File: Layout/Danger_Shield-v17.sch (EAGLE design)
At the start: 35 parts, among them U1 ARDUINO_SHIELD, U2 74LS595N, U4 TMP36

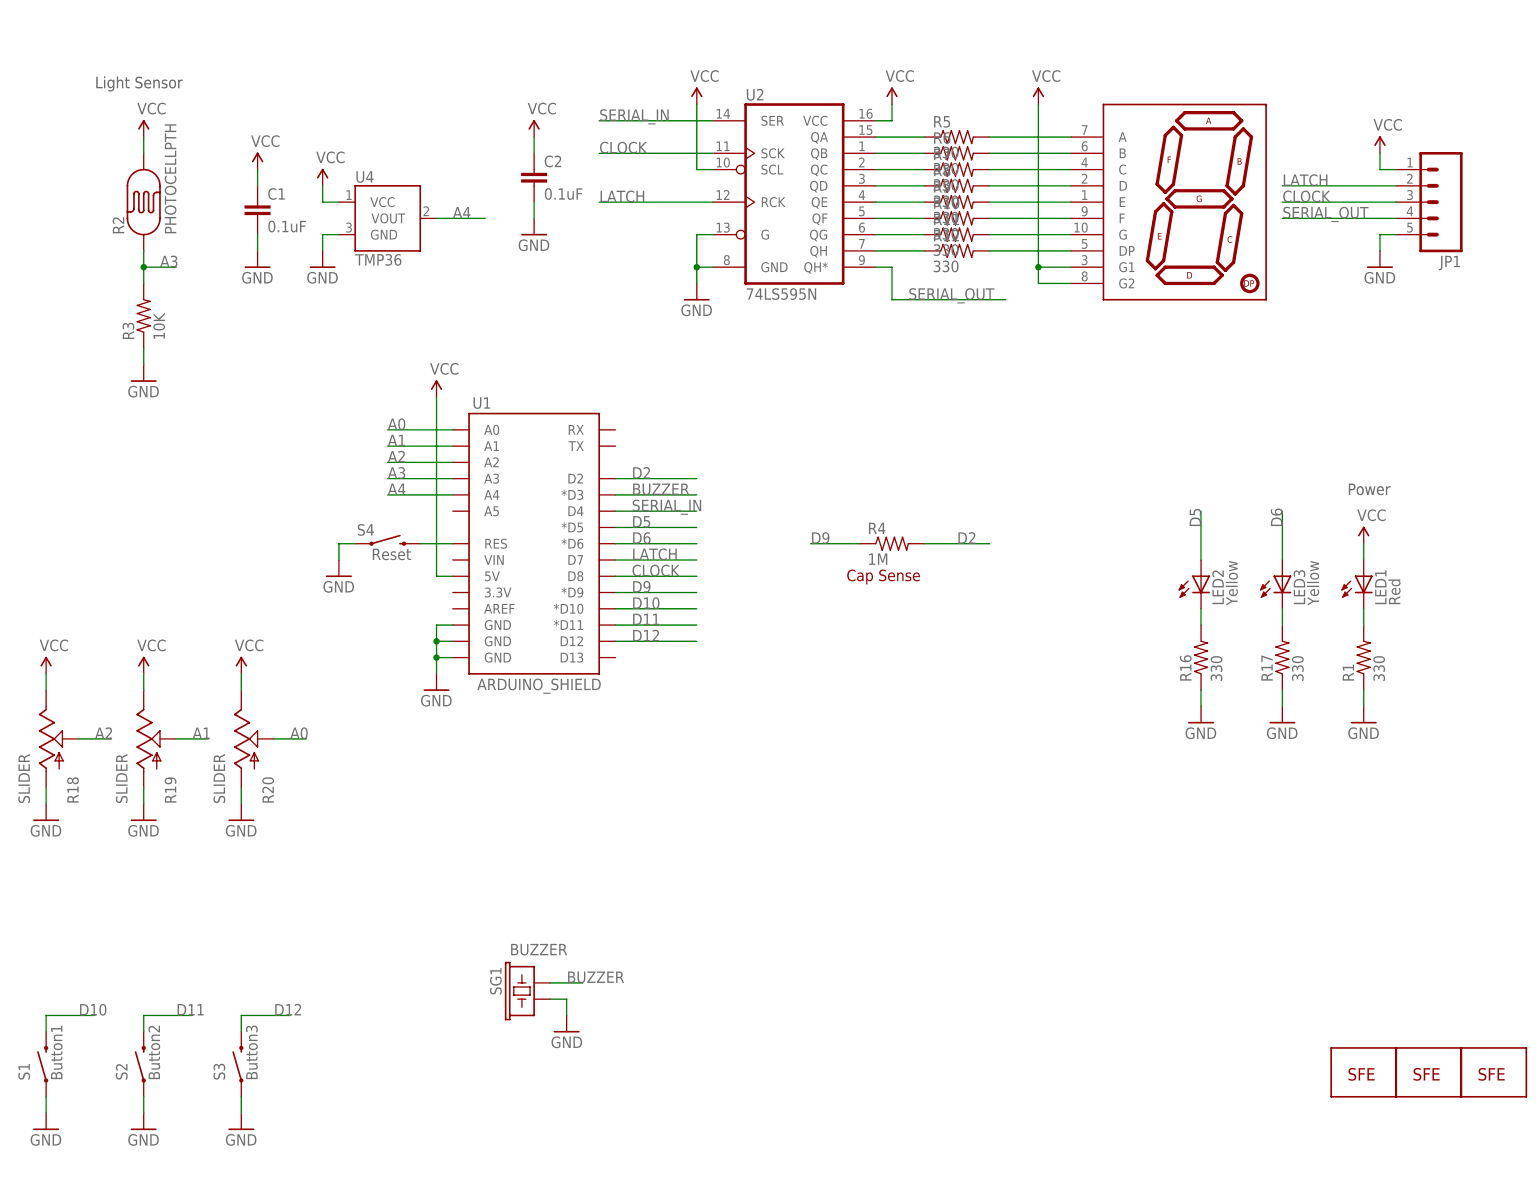
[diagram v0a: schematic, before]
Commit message: Added CC license to schematic and PCB.
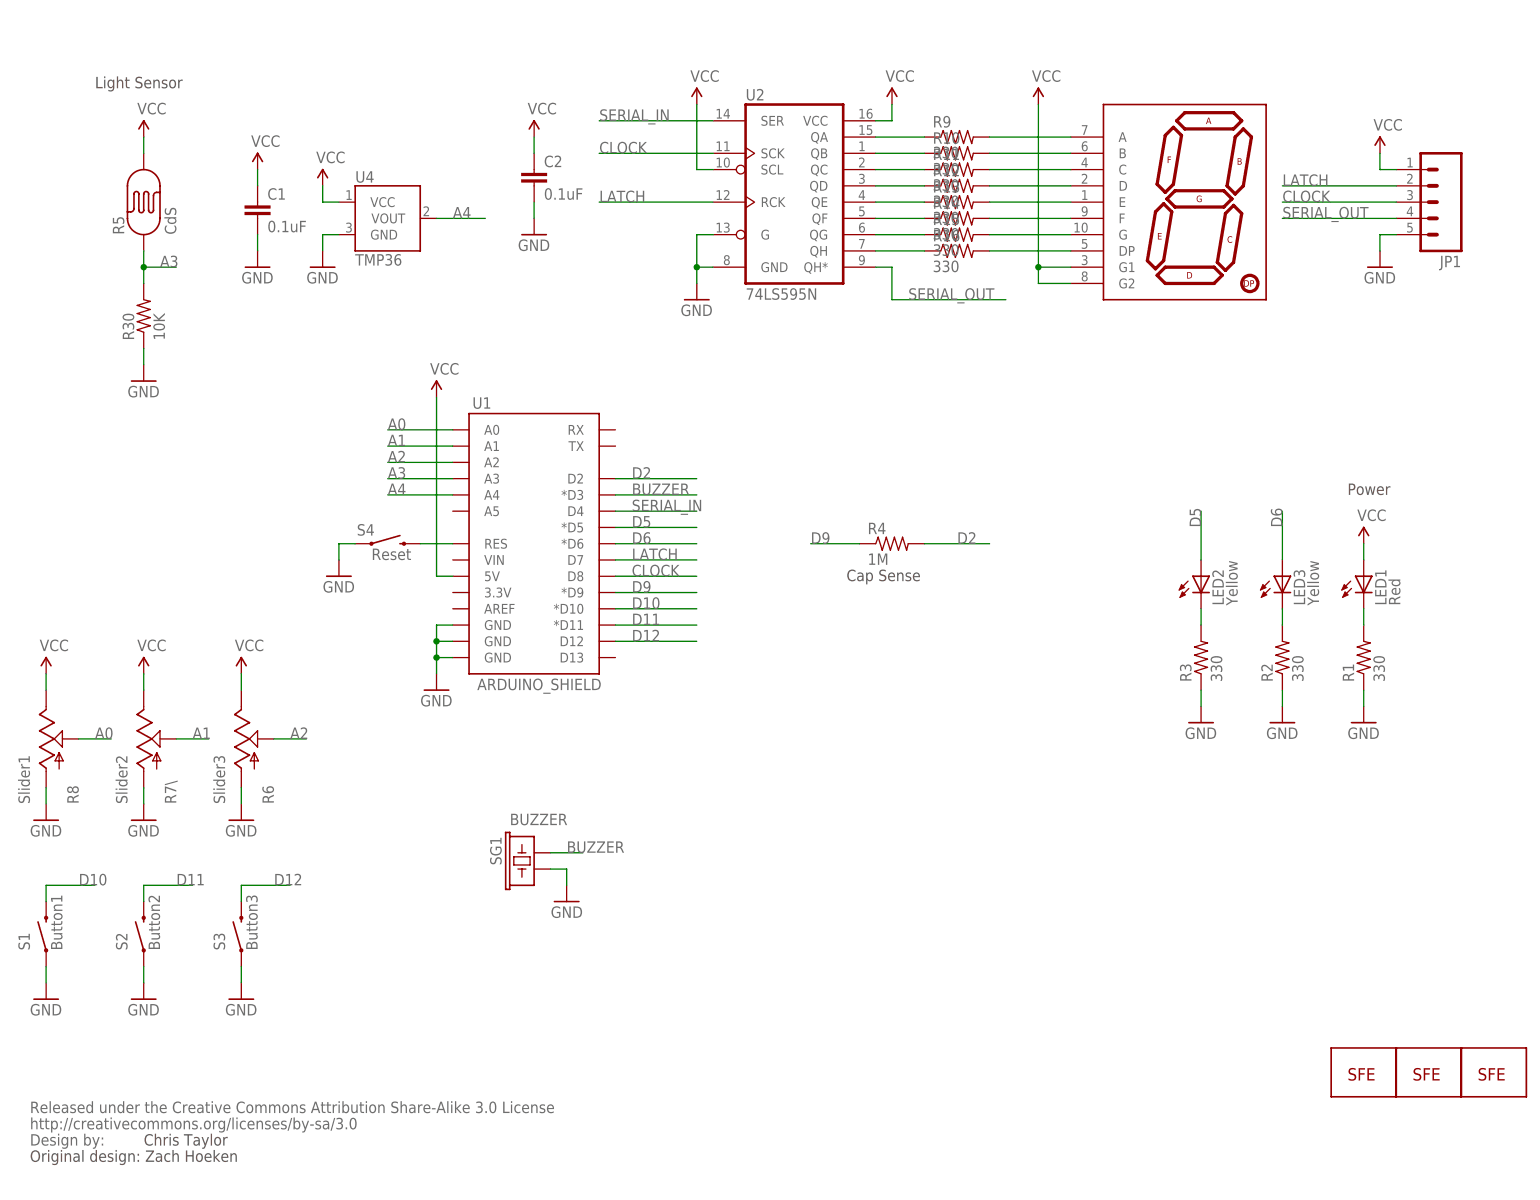
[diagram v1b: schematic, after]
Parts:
- removed R17, R7: 330, SparkFun:RESISTORAXIAL-0.3
- removed R18, R20: SLIDER, SparkFun:SLIDER
- added R13, R14, R15: 330, SparkFun:RESISTORAXIAL-0.3
- added R30: 10K, SparkFun:RESISTORAXIAL-0.3
- added U$1: CREATIVE_COMMONS, SparkFun-Aesthetics:CREATIVE_COMMONS
- R2: value PHOTOCELLPTH -> 330; device SparkFun:PHOTOCELLPTH -> SparkFun:RESISTORAXIAL-0.3
- R3: value 10K -> 330
- R5: value 330 -> CdS; device SparkFun:RESISTORAXIAL-0.3 -> SparkFun:PHOTOCELLPTH
- R6: value 330 -> Slider3; device SparkFun:RESISTORAXIAL-0.3 -> SparkFun:SLIDER
- R7\: value SLIDER -> Slider2
- R8: value 330 -> Slider1; device SparkFun:RESISTORAXIAL-0.3 -> SparkFun:SLIDER
- renumbered R19 to R7\
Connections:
- net A0: now also R8.S; no longer R20.S
- net A2: now also R6.S; no longer R18.S
- net A3: now also R30.2, R5.P$1; no longer R2.P$1, R3.2
- net GND: now also R2.1, R30.1, R6.A, R8.A; no longer R16.1, R17.1, R18.A, R20.A
- net N$10: now also R16.1; no longer R12.1
- net N$11: now also R9.2; no longer R5.2
- net N$12: now also R10.2; no longer R6.2
- net N$13: now also R11.2; no longer R7.2
- net N$14: now also R12.2; no longer R8.2
- net N$15: now also R13.2; no longer R9.2
- net N$16: now also R14.2; no longer R10.2
- net N$17: now also R15.2; no longer R11.2
- net N$18: now also R16.2; no longer R12.2
- net N$19: now also R2.2; no longer R17.2
- net N$2: now also R9.1; no longer R5.1
- net N$20: now also R3.2; no longer R16.2
- net N$4: now also R10.1; no longer R6.1
- net N$5: now also R11.1; no longer R7.1
- net N$6: now also R12.1; no longer R8.1
- net N$7: now also R13.1; no longer R9.1
- net N$8: now also R14.1; no longer R10.1
- net N$9: now also R15.1; no longer R11.1
- net VCC: now also R5.P$2, R6.E, R8.E; no longer R18.E, R2.P$2, R20.E
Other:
- note added: "Chris Taylor"
- note added: "Original design: Zach Hoeken"
- moved on the sheet: R10, R11, R12, R16, R3, R9, S1, S2, S3, SG1

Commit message: Update to gitignore. Added OSHW logo. Fixed overlapping resistors.
Cleaned up the example code slightly as well. Trying to fit into
SparkFun coding standards.
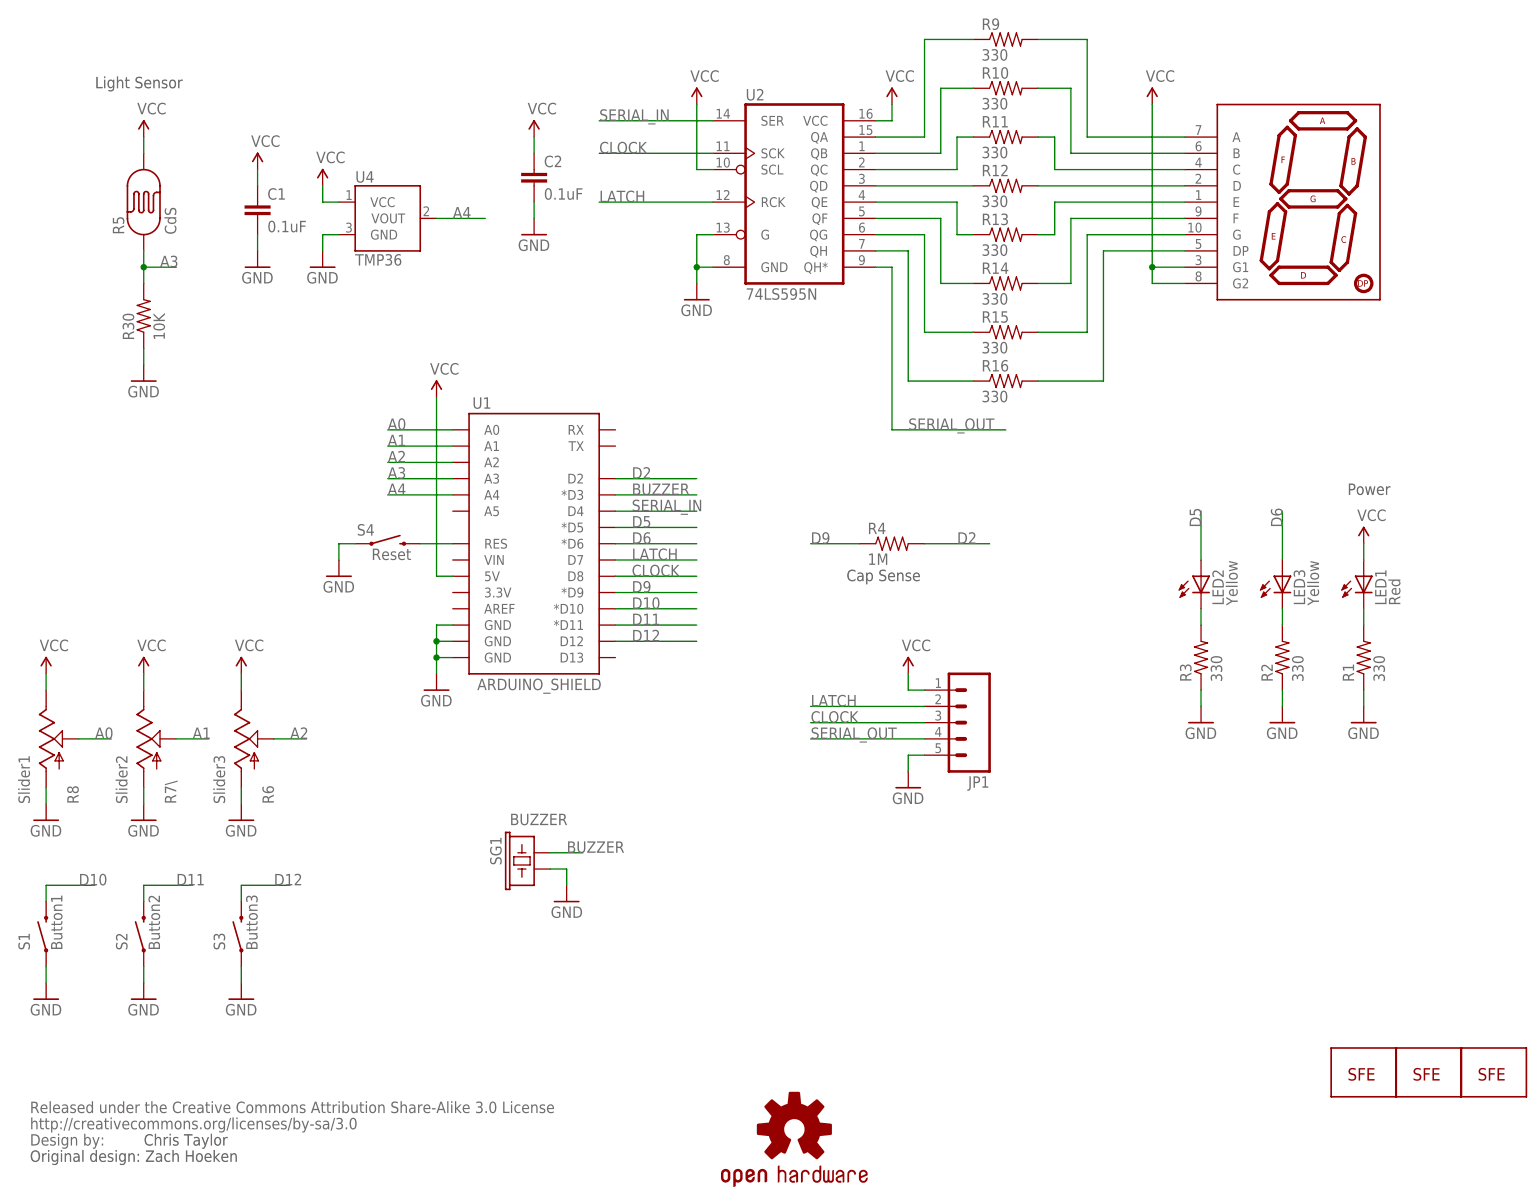
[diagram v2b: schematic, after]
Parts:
- added U$2: OSHW-LOGOM, SparkFun-Aesthetics:OSHW-LOGOM
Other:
- moved on the sheet: JP1, R10, R11, R12, R13, R14, R15, R16, R9

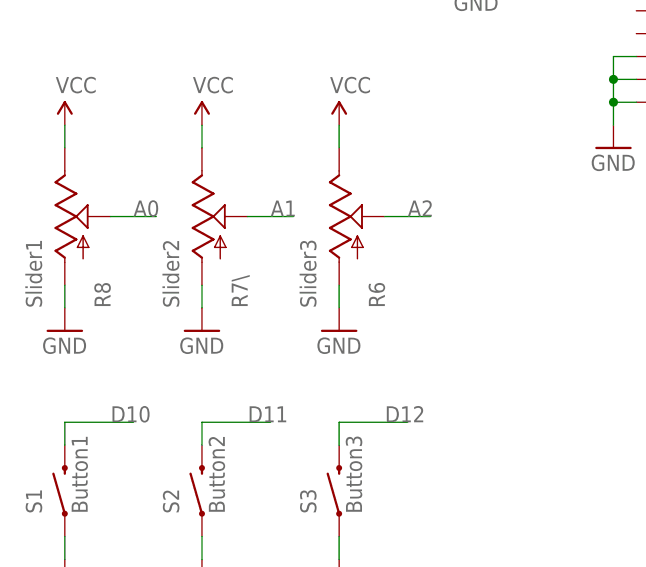
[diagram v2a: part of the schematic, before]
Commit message: Adding dimensional and BOM.
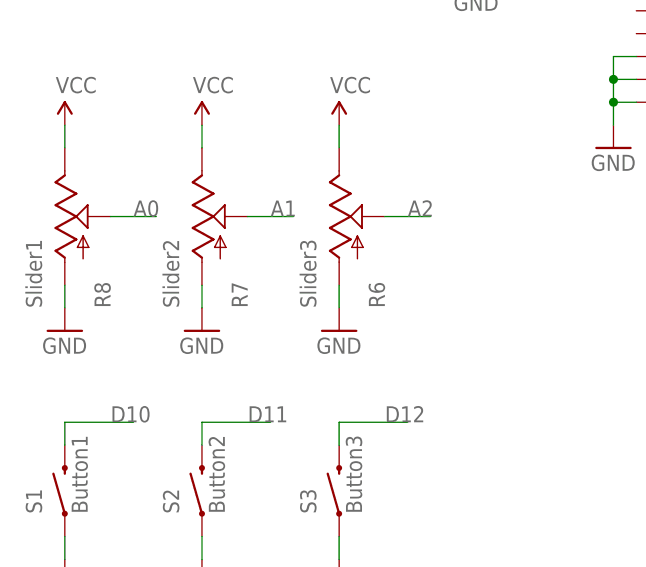
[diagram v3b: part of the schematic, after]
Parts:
- renumbered R7\ to R7, U$6 to U6
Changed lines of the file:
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@@
 <part name="R8" library="SparkFun" deviceset="SLIDER" device="" value="Slider1"/>
 <part name="FRAME1" library="SparkFun" deviceset="FRAME-LETTER" device=""/>
-<part name="R7\" library="SparkFun" deviceset="SLIDER" device="" value="Slider2"/>
+<part name="R7" library="SparkFun" deviceset="SLIDER" device="" value="Slider2"/>
 <part name="R6" library="SparkFun" deviceset="SLIDER" device="" value="Slider3"/>
 <part name="P+1" library="SparkFun" deviceset="VCC" device=""/>
@@
 <part name="JP3" library="SparkFun" deviceset="LOGO-SFE" device="NEW"/>
 <part name="JP5" library="SparkFun" deviceset="LOGO-SFE" device="SK"/>
-<part name="U$6" library="SparkFun" deviceset="7-SEGMENT-DISPLAY-1&quot;-RED" device=""/>
+<part name="U6" library="SparkFun" deviceset="7-SEGMENT-DISPLAY-1&quot;-RED" device=""/>
 <part name="S2" library="SparkFun" deviceset="SWITCH-MOMENTARY-2" device="12MM" value="Button2"/>
 <part name="S1" library="SparkFun" deviceset="SWITCH-MOMENTARY-2" device="12MM" value="Button1"/>
@@
 <instance part="FRAME1" gate="G$1" x="0" y="0"/>
 <instance part="FRAME1" gate="G$2" x="147.32" y="0"/>
-<instance part="R7\" gate="G$1" x="33.02" y="71.12"/>
+<instance part="R7" gate="G$1" x="33.02" y="71.12"/>
 <instance part="R6" gate="G$1" x="48.26" y="71.12"/>
 <instance part="P+1" gate="1" x="48.26" y="81.28"/>
@@
 <instance part="JP3" gate="G$1" x="220.98" y="17.78"/>
 <instance part="JP5" gate="G$1" x="241.3" y="17.78"/>
-<instance part="U$6" gate="G$1" x="215.9" y="154.94"/>
+<instance part="U6" gate="G$1" x="215.9" y="154.94"/>
 <instance part="S2" gate="G$1" x="33.02" y="40.64" rot="R90"/>
 <instance part="S1" gate="G$1" x="17.78" y="40.64" rot="R90"/>
@@
 <segment>
 <wire x1="33.02" y1="78.74" x2="33.02" y2="81.28" width="0.1524" layer="91"/>
-<pinref part="R7\" gate="G$1" pin="E"/>
+<pinref part="R7" gate="G$1" pin="E"/>
 <pinref part="P+2" gate="1" pin="VCC"/>
 </segment>
@@
 <wire x1="190.5" y1="142.24" x2="190.5" y2="144.78" width="0.1524" layer="91"/>
 <junction x="190.5" y="144.78"/>
-<pinref part="U$6" gate="G$1" pin="G1"/>
+<pinref part="U6" gate="G$1" pin="G1"/>
 <pinref part="P+13" gate="1" pin="VCC"/>
-<pinref part="U$6" gate="G$1" pin="G2"/>
+<pinref part="U6" gate="G$1" pin="G2"/>
 </segment>
 <segment>
@@
 <wire x1="33.02" y1="60.96" x2="33.02" y2="63.5" width="0.1524" layer="91"/>
 <pinref part="GND2" gate="1" pin="GND"/>
-<pinref part="R7\" gate="G$1" pin="A"/>
+<pinref part="R7" gate="G$1" pin="A"/>
 </segment>
 <segment>
@@
 <wire x1="38.1" y1="71.12" x2="43.18" y2="71.12" width="0.1524" layer="91"/>
 <label x="40.64" y="71.12" size="1.778" layer="95"/>
-<pinref part="R7\" gate="G$1" pin="S"/>
+<pinref part="R7" gate="G$1" pin="S"/>
 </segment>
 <segment>
@@
 <wire x1="180.34" y1="180.34" x2="172.72" y2="180.34" width="0.1524" layer="91"/>
 <pinref part="R9" gate="G$1" pin="2"/>
-<pinref part="U$6" gate="G$1" pin="A"/>
+<pinref part="U6" gate="G$1" pin="A"/>
 </segment>
 </net>
@@
 <wire x1="177.8" y1="172.72" x2="172.72" y2="172.72" width="0.1524" layer="91"/>
 <pinref part="R10" gate="G$1" pin="2"/>
-<pinref part="U$6" gate="G$1" pin="B"/>
+<pinref part="U6" gate="G$1" pin="B"/>
 </segment>
 </net>
@@
 <wire x1="175.26" y1="165.1" x2="172.72" y2="165.1" width="0.1524" layer="91"/>
 <pinref part="R11" gate="G$1" pin="2"/>
-<pinref part="U$6" gate="G$1" pin="C"/>
+<pinref part="U6" gate="G$1" pin="C"/>
 </segment>
 </net>
@@
 <wire x1="195.58" y1="157.48" x2="172.72" y2="157.48" width="0.1524" layer="91"/>
 <pinref part="R12" gate="G$1" pin="2"/>
-<pinref part="U$6" gate="G$1" pin="D"/>
+<pinref part="U6" gate="G$1" pin="D"/>
 </segment>
 </net>
@@
 <wire x1="175.26" y1="149.86" x2="172.72" y2="149.86" width="0.1524" layer="91"/>
 <pinref part="R13" gate="G$1" pin="2"/>
-<pinref part="U$6" gate="G$1" pin="E"/>
+<pinref part="U6" gate="G$1" pin="E"/>
 </segment>
 </net>
@@
 <wire x1="177.8" y1="142.24" x2="172.72" y2="142.24" width="0.1524" layer="91"/>
 <pinref part="R14" gate="G$1" pin="2"/>
-<pinref part="U$6" gate="G$1" pin="F"/>
+<pinref part="U6" gate="G$1" pin="F"/>
 </segment>
 </net>
@@
 <wire x1="180.34" y1="134.62" x2="172.72" y2="134.62" width="0.1524" layer="91"/>
 <pinref part="R15" gate="G$1" pin="2"/>
-<pinref part="U$6" gate="G$1" pin="G"/>
+<pinref part="U6" gate="G$1" pin="G"/>
 </segment>
 </net>
@@
 <wire x1="182.88" y1="127" x2="172.72" y2="127" width="0.1524" layer="91"/>
 <pinref part="R16" gate="G$1" pin="2"/>
-<pinref part="U$6" gate="G$1" pin="DP"/>
-</segment>
-</net>
+<pinref part="U6" gate="G$1" pin="DP"/>
+</segment>
+</net>
